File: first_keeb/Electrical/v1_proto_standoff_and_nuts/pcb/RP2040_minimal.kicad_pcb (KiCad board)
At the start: 4 copper layers, 67.1 x 66.8 mm, 86 parts, among them J1 Conn_01x04_Socket, J2 Conn_01x04_Socket, P1 USB-TYPE-C-016, Q1 SN74LV1T34DBV, SW1 SKRKAHE020, SW2 SKRKAHE020, SW3 BUTT1, SW4 BUTT3, SW5 BUTT2, U1 AMS1117-2.5, U2 ME6208A44M3G, U3 PRTR5V0U2X, U4 STM32F401RCTx, U5 MCP6001-OT, U6 MCP6001-OT, Y1 16MHz

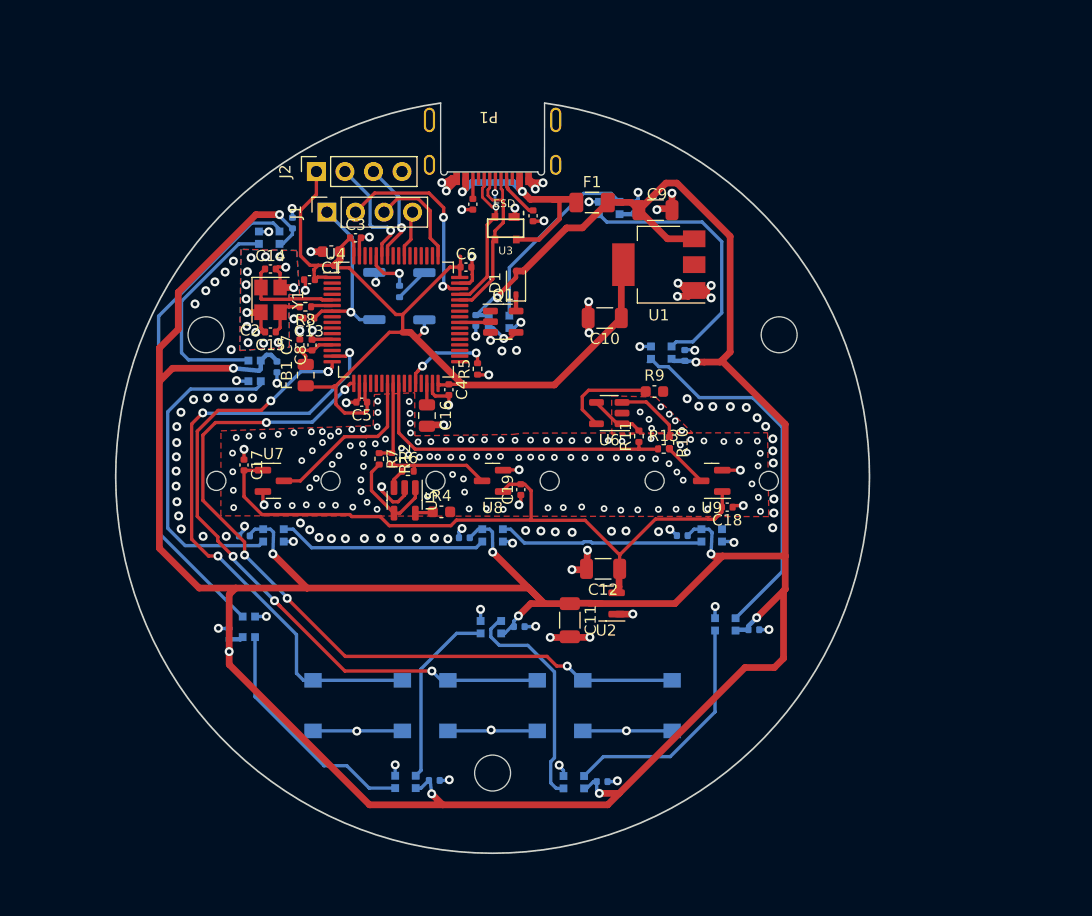
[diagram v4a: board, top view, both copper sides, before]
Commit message: finishes pcb v1 with smaller radius
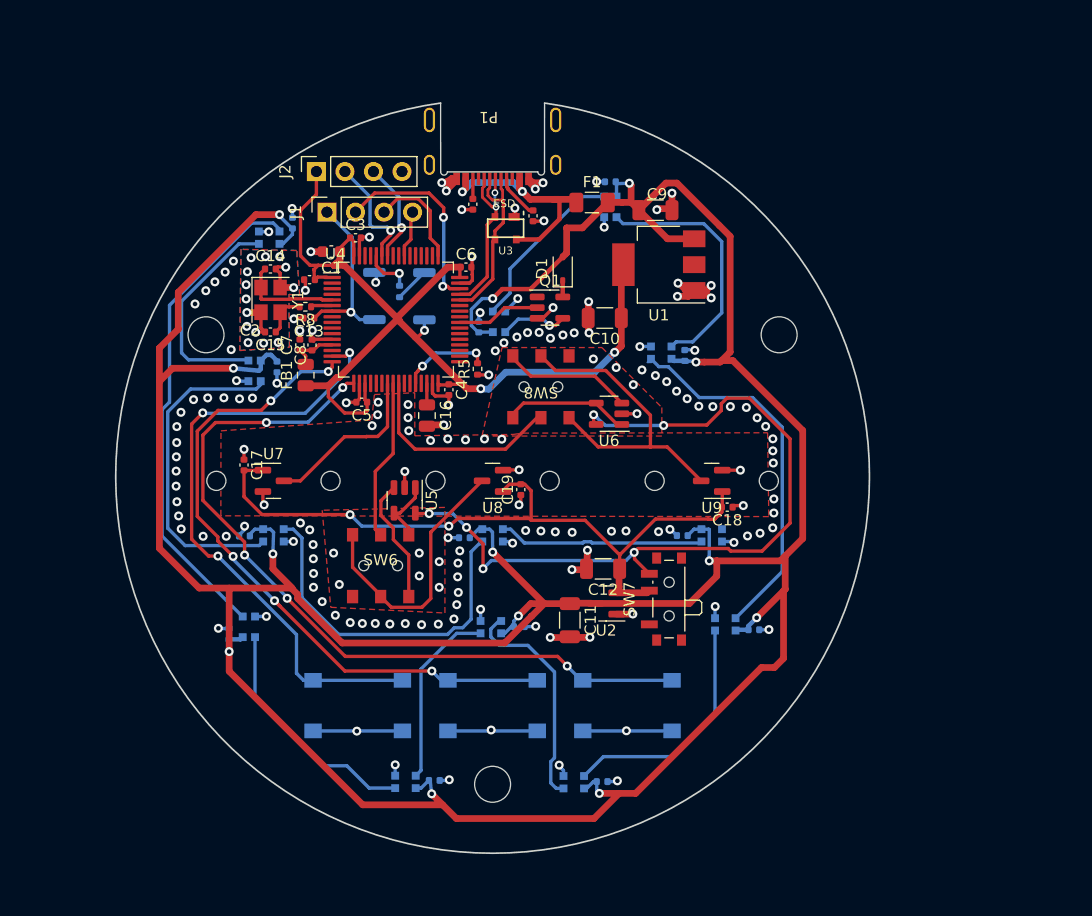
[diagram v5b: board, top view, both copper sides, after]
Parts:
- removed R10, R11, R6, R7: DNP, Resistor_SMD:R_0402_1005Metric
- removed R12, R13: 0, Resistor_SMD:R_0402_1005Metric
- removed R4, R9: DNP, Capacitor_SMD:C_0603_1608Metric
- added SW6: MS-22C01-G010, Button_Switch_SMD:DPDT-MS-22C01, F.Cu at (90.0, 107.5)
- added SW7: SK-3296S-01-L3, Button_Switch_SMD:SW_SPDT_PCM12, F.Cu at (115.4, 110.5)
- added SW8: MS-22C01-G010, Button_Switch_SMD:DPDT-MS-22C01, F.Cu at (104.3, 91.6)
- moved Q1 4.34 mm to (105.1, 84.6)
- moved D1 4.34 mm to (106.2, 81.1)
- moved C21 3.16 mm to (110.5, 73.4), turned to 180 degrees
- moved H3 1.00 mm to (100.0, 127.0)
- moved C20 0.64 mm to (98.8, 86.3), turned to 90 degrees
- moved D3 0.14 mm to (110.5, 75.6), turned to 90 degrees
- moved U6 0.06 mm to (110.4, 94.0)
- turned D2 to -90 degrees
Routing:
- net V_test: track 0.00 -> 70.9 mm, vias 0 -> 6
- net S_ADC_IN3: track 0.00 -> 29.2 mm
- net S_ADC_IN2: track 0.00 -> 24.1 mm
- net Net-(D12-DOUT): track 18.6 -> 31.6 mm
- net +5V: track 311.2 -> 324.1 mm, vias 12 -> 13
- net O_ADC_IN3: track 0.00 -> 11.0 mm
- net ADC_IN3: track 29.0 -> 18.9 mm
- net Net-(U5--): track 9.23 -> 0.00 mm
- net Net-(U6-V+): track 8.60 -> 0.00 mm
- net ALT_ADC_3: track 4.01 -> 11.9 mm
- net ADC_IN2: track 7.44 -> 14.3 mm
- net O_ADC_IN2: track 0.00 -> 6.26 mm
- net Net-(U6-+): track 6.14 -> 0.00 mm
- net Net-(U6--): track 4.84 -> 0.00 mm
- net LED_D: track 2.76 -> 7.44 mm
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
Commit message: cleanup tracks and vias
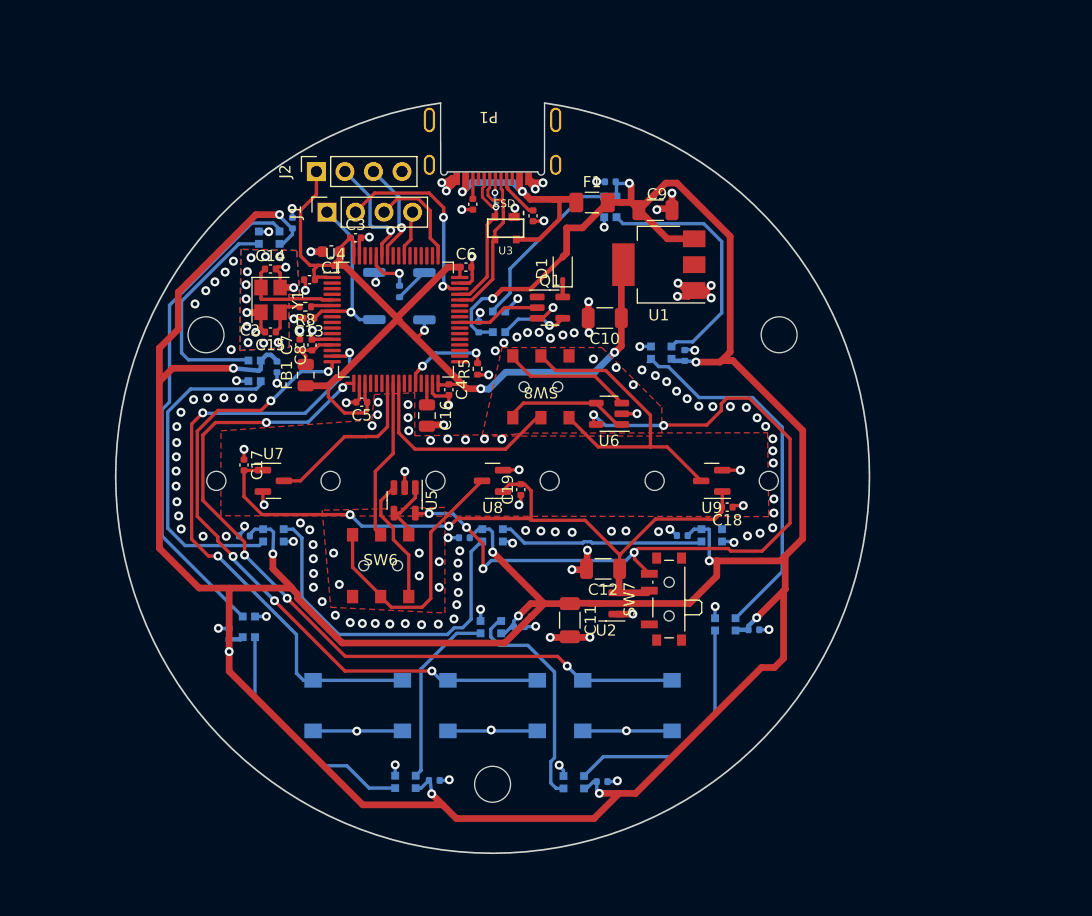
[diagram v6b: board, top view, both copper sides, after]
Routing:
- net +5V: track 324.1 -> 322.7 mm
- net GND: track 124.2 -> 123.0 mm
- net O_ADC_IN2: track 6.26 -> 5.37 mm
- net BUTT1: track 60.3 -> 59.6 mm
- net Net-(U4-VCAP1): track 2.37 -> 1.64 mm
- net VDD: track 89.0 -> 88.3 mm
- net V_test: track 70.9 -> 70.3 mm
- net ALT_ADC_2: track 11.7 -> 11.2 mm

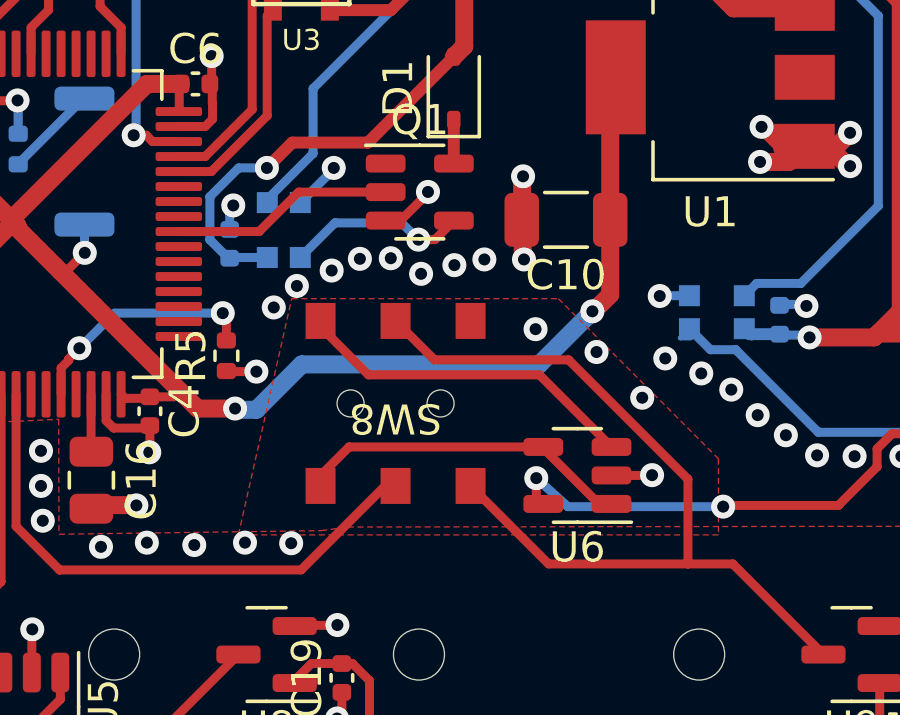
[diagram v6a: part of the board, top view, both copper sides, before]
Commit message: improve power routing to go around analog signals
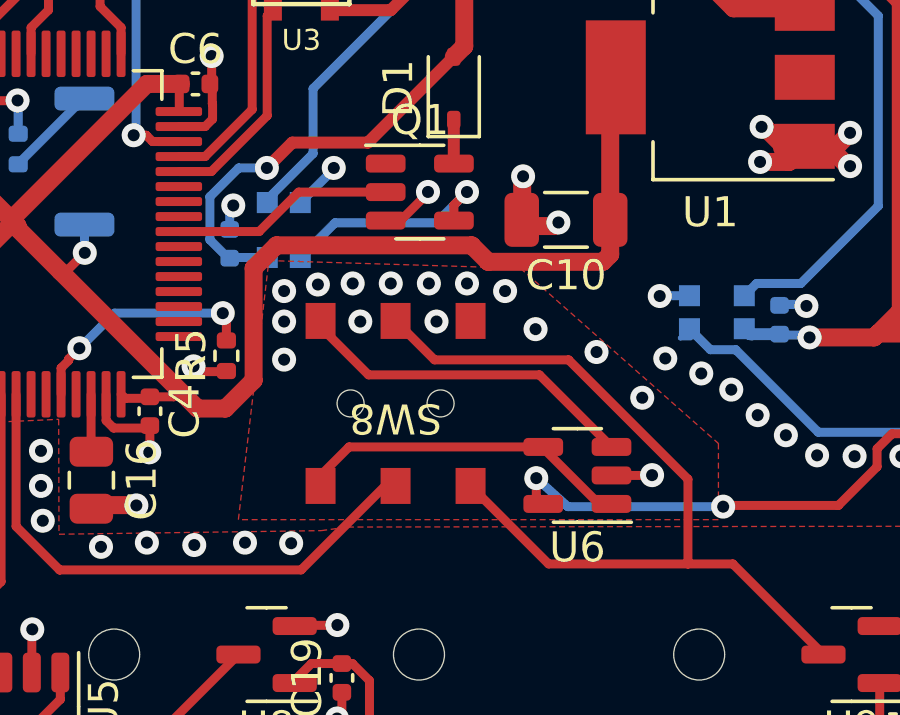
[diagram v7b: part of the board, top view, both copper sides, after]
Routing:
- net VDD: track 88.3 -> 90.1 mm, vias 3 -> 1
- net Net-(D2-DIN): track 6.09 -> 7.59 mm
- net GND: vias 181 -> 184

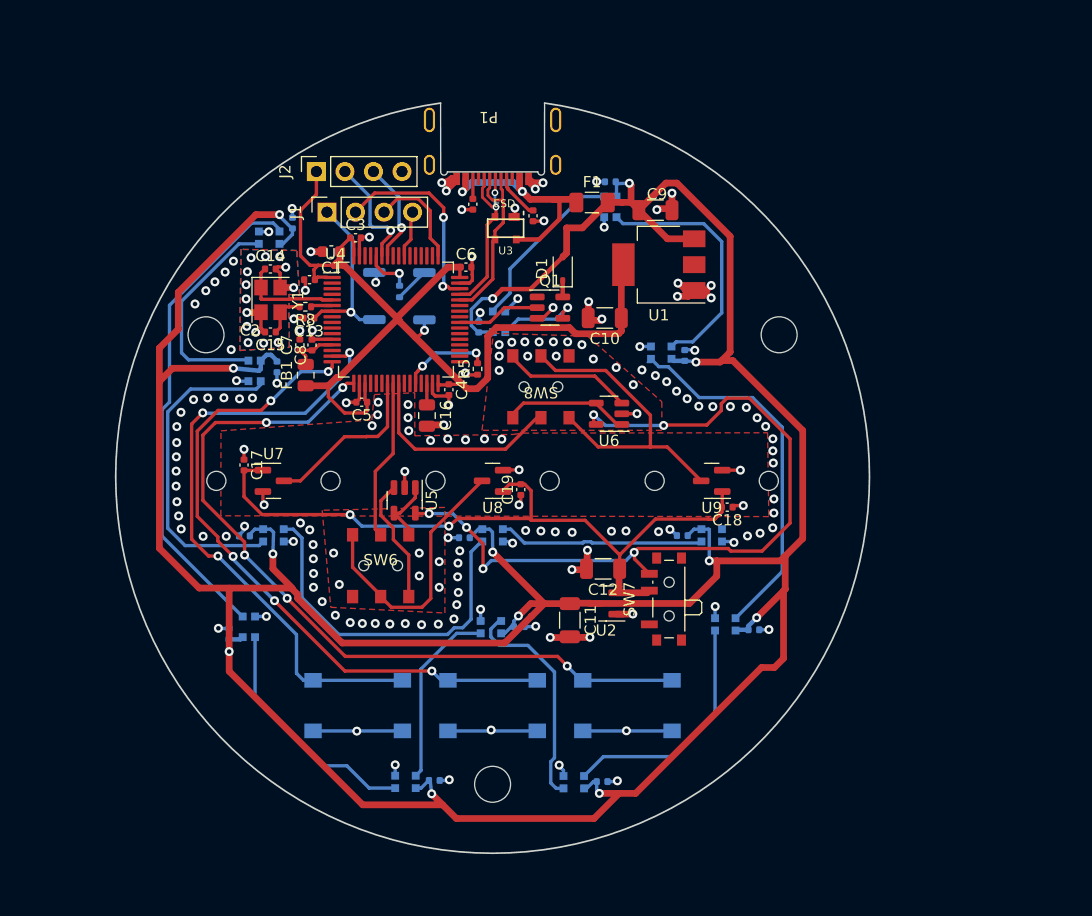
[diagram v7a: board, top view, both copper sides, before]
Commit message: generate prod files for pcb
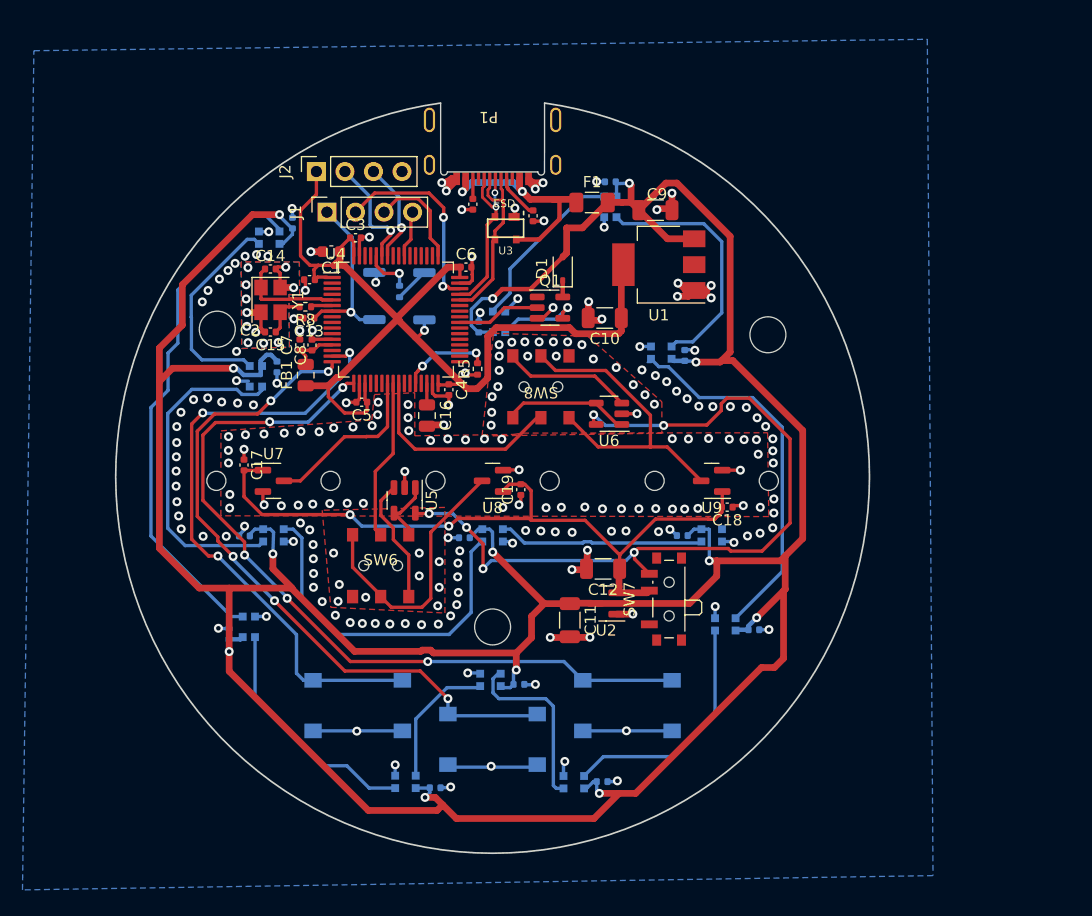
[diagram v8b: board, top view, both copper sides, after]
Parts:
- moved H3 14.0 mm to (100.0, 113.0)
- moved C25 5.14 mm to (102.3, 118.1)
- moved D7 4.69 mm to (99.8, 117.7)
- moved SW5 3.00 mm to (100.0, 123.0)
- moved H2 1.12 mm to (75.5, 86.5)
- moved H1 1.00 mm to (124.5, 87.0)
- moved C26 0.65 mm to (94.9, 127.3)
- moved D11 0.49 mm to (78.9, 90.7)
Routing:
- net Net-(D7-DOUT): track 16.3 -> 12.0 mm
- net Net-(D6-DOUT): track 20.2 -> 16.1 mm
- net Net-(D10-DIN): track 44.2 -> 46.5 mm
- net BUTT1: track 59.6 -> 61.8 mm
- net +5V: track 322.7 -> 324.7 mm
- net Net-(D10-DOUT): track 19.8 -> 18.9 mm
- net GND: track 123.0 -> 123.2 mm, vias 184 -> 230
